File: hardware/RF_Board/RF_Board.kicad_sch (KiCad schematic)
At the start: 129 parts, among them J1 Conn_Coaxial, J2 Conn_01x04_Male, J3 Conn_Coaxial, J4 Conn_01x04_Male, J5 Conn_01x06_Female, J6 Conn_01x06_Female, J7 Conn_01x06_Female, J8 L77TSAH15SOL2RM8, J9 Conn_01x09_Male, Q1 2N7002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

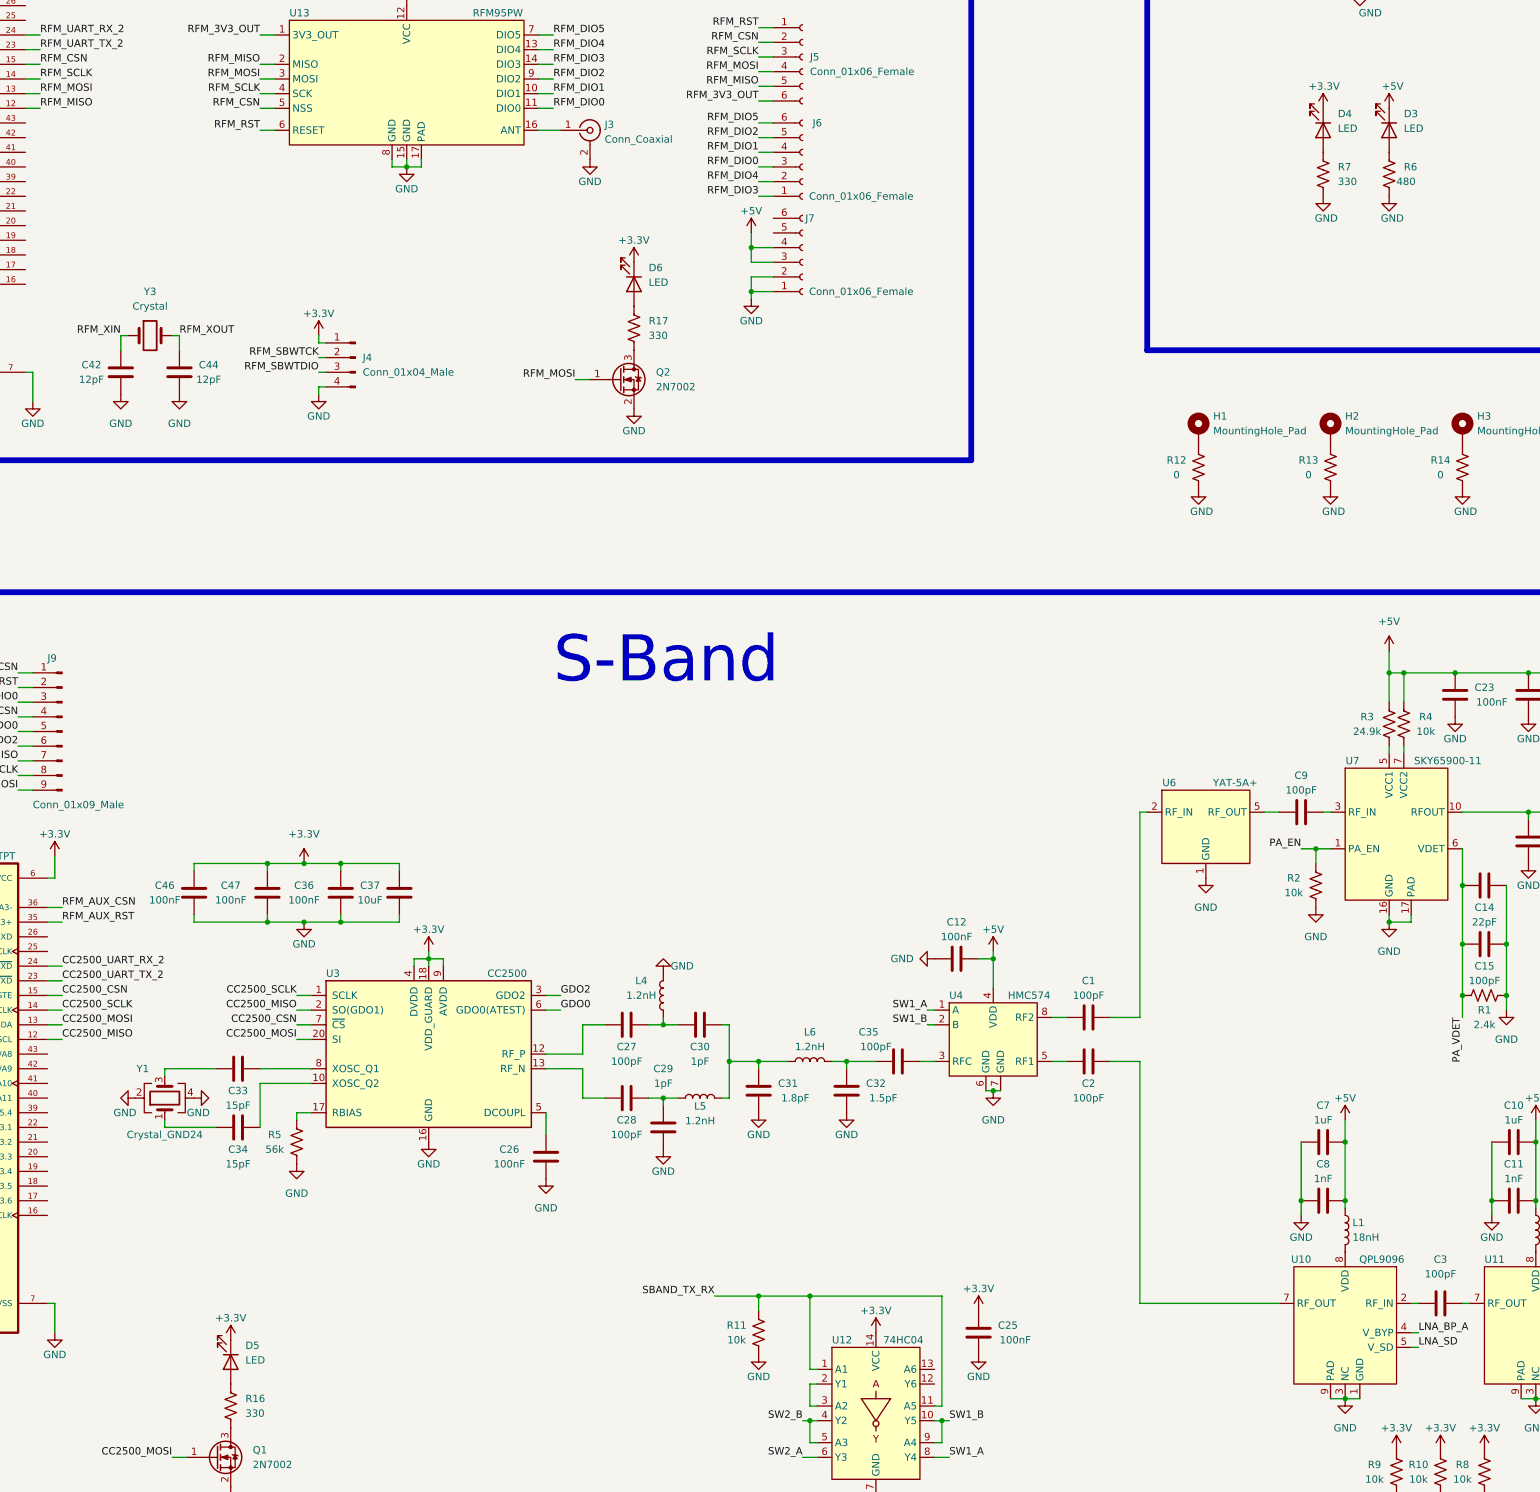
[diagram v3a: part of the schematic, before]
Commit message: fix LED polarity
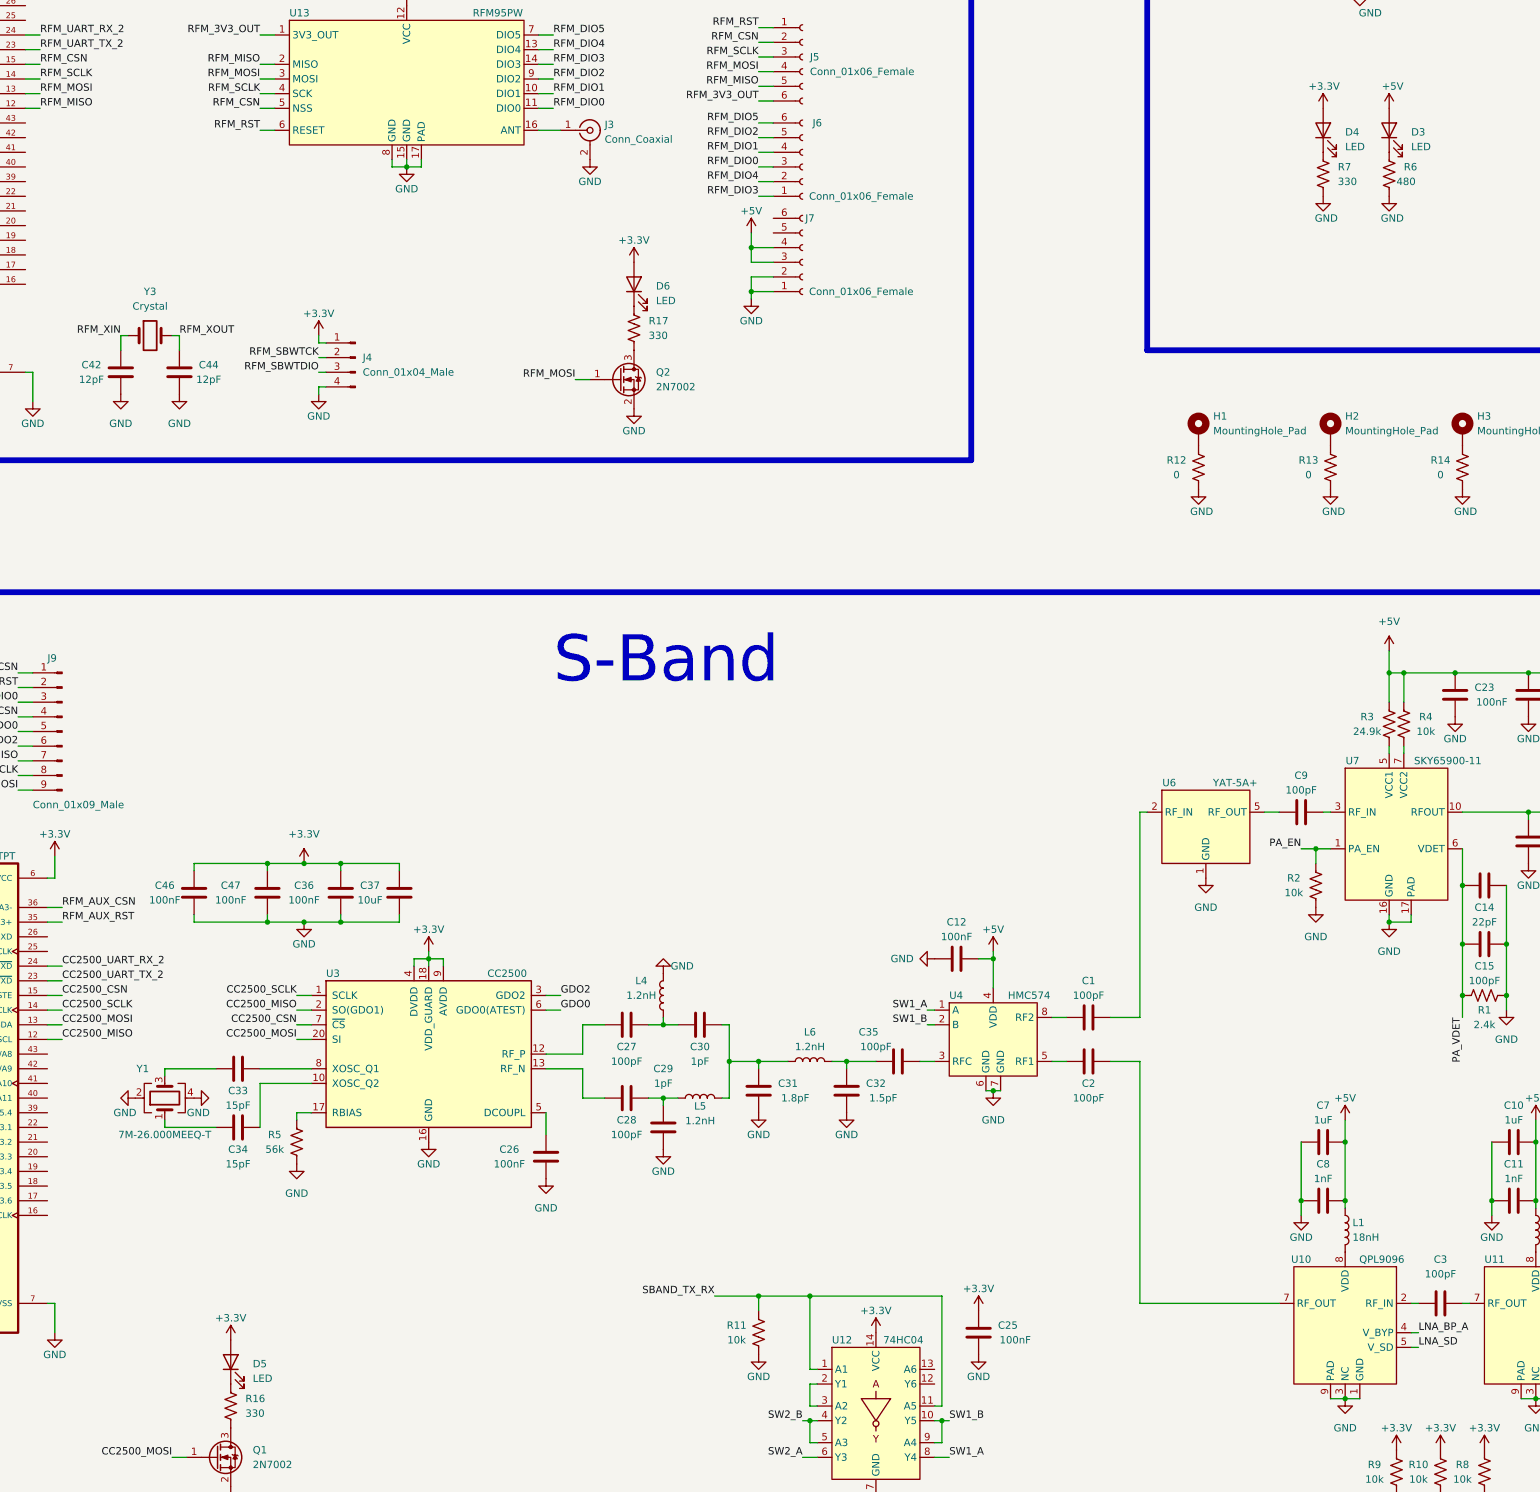
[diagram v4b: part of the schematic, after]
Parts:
- Y1: value Crystal_GND24 -> 7M-26.000MEEQ-T
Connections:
- net +3.3V: now also D4.2 (A), D5.2 (A), D6.2 (A); no longer D4.1 (K), D5.1 (K), D6.1 (K)
- net +5V: now also D3.2 (A); no longer D3.1 (K)
- net at R6.1: now also D3.1 (K); no longer D3.2 (A)
- net at R16.1: now also D5.1 (K); no longer D5.2 (A)
- net at R7.1: now also D4.1 (K); no longer D4.2 (A)
- net at R17.1: now also D6.1 (K); no longer D6.2 (A)
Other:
- moved on the sheet: D3, D4, D5, D6
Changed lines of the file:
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@@
     (pin "2")
   )
-  (symbol (lib_id "RF_Board_Symbols:LED") (at 422.91 101.6 270) (unit 1)
+  (symbol (lib_id "RF_Board_Symbols:LED") (at 422.91 101.6 90) (unit 1)
     (in_bom yes) (on_board yes) (fields_autoplaced)
-    (property "Reference" "D3" (id 0) (at 425.45 98.7424 90)
-      (effects (font (size 1.27 1.27)) (justify left))
+    (property "Reference" "D3" (id 0) (at 426.72 101.9174 90)
+      (effects (font (size 1.27 1.27)) (justify right))
     )
-    (property "Value" "LED" (id 1) (at 425.45 101.2824 90)
-      (effects (font (size 1.27 1.27)) (justify left))
+    (property "Value" "LED" (id 1) (at 426.72 104.4574 90)
+      (effects (font (size 1.27 1.27)) (justify right))
     )
     (property "Footprint" "RF_Board_Footprints:LED_0603_1608Metric" (id 2) (at 422.91 101.6 0)
@@
     (in_bom yes) (on_board yes)
     (property "Reference" "Y1" (id 0) (at 207.01 264.16 90))
-    (property "Value" "Crystal_GND24" (id 1) (at 210.82 275.59 90))
+    (property "Value" "7M-26.000MEEQ-T" (id 1) (at 210.82 275.59 90))
     (property "Footprint" "RF_Board_Footprints:Crystal_SMD_3225-4Pin_3.2x2.5mm" (id 2) (at 210.82 269.24 0)
       (effects (font (size 1.27 1.27)) hide)
@@
     (pin "2")
   )
-  (symbol (lib_id "RF_Board_Symbols:LED") (at 411.48 101.6 270) (unit 1)
+  (symbol (lib_id "RF_Board_Symbols:LED") (at 411.48 101.6 90) (unit 1)
     (in_bom yes) (on_board yes) (fields_autoplaced)
-    (property "Reference" "D4" (id 0) (at 414.02 98.7424 90)
-      (effects (font (size 1.27 1.27)) (justify left))
+    (property "Reference" "D4" (id 0) (at 415.29 101.9174 90)
+      (effects (font (size 1.27 1.27)) (justify right))
     )
-    (property "Value" "LED" (id 1) (at 414.02 101.2824 90)
-      (effects (font (size 1.27 1.27)) (justify left))
+    (property "Value" "LED" (id 1) (at 415.29 104.4574 90)
+      (effects (font (size 1.27 1.27)) (justify right))
     )
     (property "Footprint" "RF_Board_Footprints:LED_0603_1608Metric" (id 2) (at 411.48 101.6 0)
@@
     (pin "1")
   )
-  (symbol (lib_id "RF_Board_Symbols:LED") (at 292.1 128.27 270) (unit 1)
+  (symbol (lib_id "RF_Board_Symbols:LED") (at 292.1 128.27 90) (unit 1)
     (in_bom yes) (on_board yes) (fields_autoplaced)
-    (property "Reference" "D6" (id 0) (at 294.64 125.4124 90)
-      (effects (font (size 1.27 1.27)) (justify left))
+    (property "Reference" "D6" (id 0) (at 295.91 128.5874 90)
+      (effects (font (size 1.27 1.27)) (justify right))
     )
-    (property "Value" "LED" (id 1) (at 294.64 127.9524 90)
-      (effects (font (size 1.27 1.27)) (justify left))
+    (property "Value" "LED" (id 1) (at 295.91 131.1274 90)
+      (effects (font (size 1.27 1.27)) (justify right))
     )
     (property "Footprint" "RF_Board_Footprints:LED_0603_1608Metric" (id 2) (at 292.1 128.27 0)
@@
     (pin "2")
   )
-  (symbol (lib_id "RF_Board_Symbols:LED") (at 222.25 314.96 270) (unit 1)
+  (symbol (lib_id "RF_Board_Symbols:LED") (at 222.25 314.96 90) (unit 1)
     (in_bom yes) (on_board yes) (fields_autoplaced)
-    (property "Reference" "D5" (id 0) (at 224.79 312.1024 90)
-      (effects (font (size 1.27 1.27)) (justify left))
+    (property "Reference" "D5" (id 0) (at 226.06 315.2774 90)
+      (effects (font (size 1.27 1.27)) (justify right))
     )
-    (property "Value" "LED" (id 1) (at 224.79 314.6424 90)
-      (effects (font (size 1.27 1.27)) (justify left))
+    (property "Value" "LED" (id 1) (at 226.06 317.8174 90)
+      (effects (font (size 1.27 1.27)) (justify right))
     )
     (property "Footprint" "RF_Board_Footprints:LED_0603_1608Metric" (id 2) (at 222.25 314.96 0)
@@
     )
     (path "/2e2c2d33-fba7-4ab8-92e0-d611208419ce"
-      (reference "Y1") (unit 1) (value "Crystal_GND24") (footprint "RF_Board_Footprints:Crystal_SMD_3225-4Pin_3.2x2.5mm")
+      (reference "Y1") (unit 1) (value "7M-26.000MEEQ-T") (footprint "RF_Board_Footprints:Crystal_SMD_3225-4Pin_3.2x2.5mm")
     )
     (path "/b1e13d1d-1049-4af9-bbdf-669677daba83"

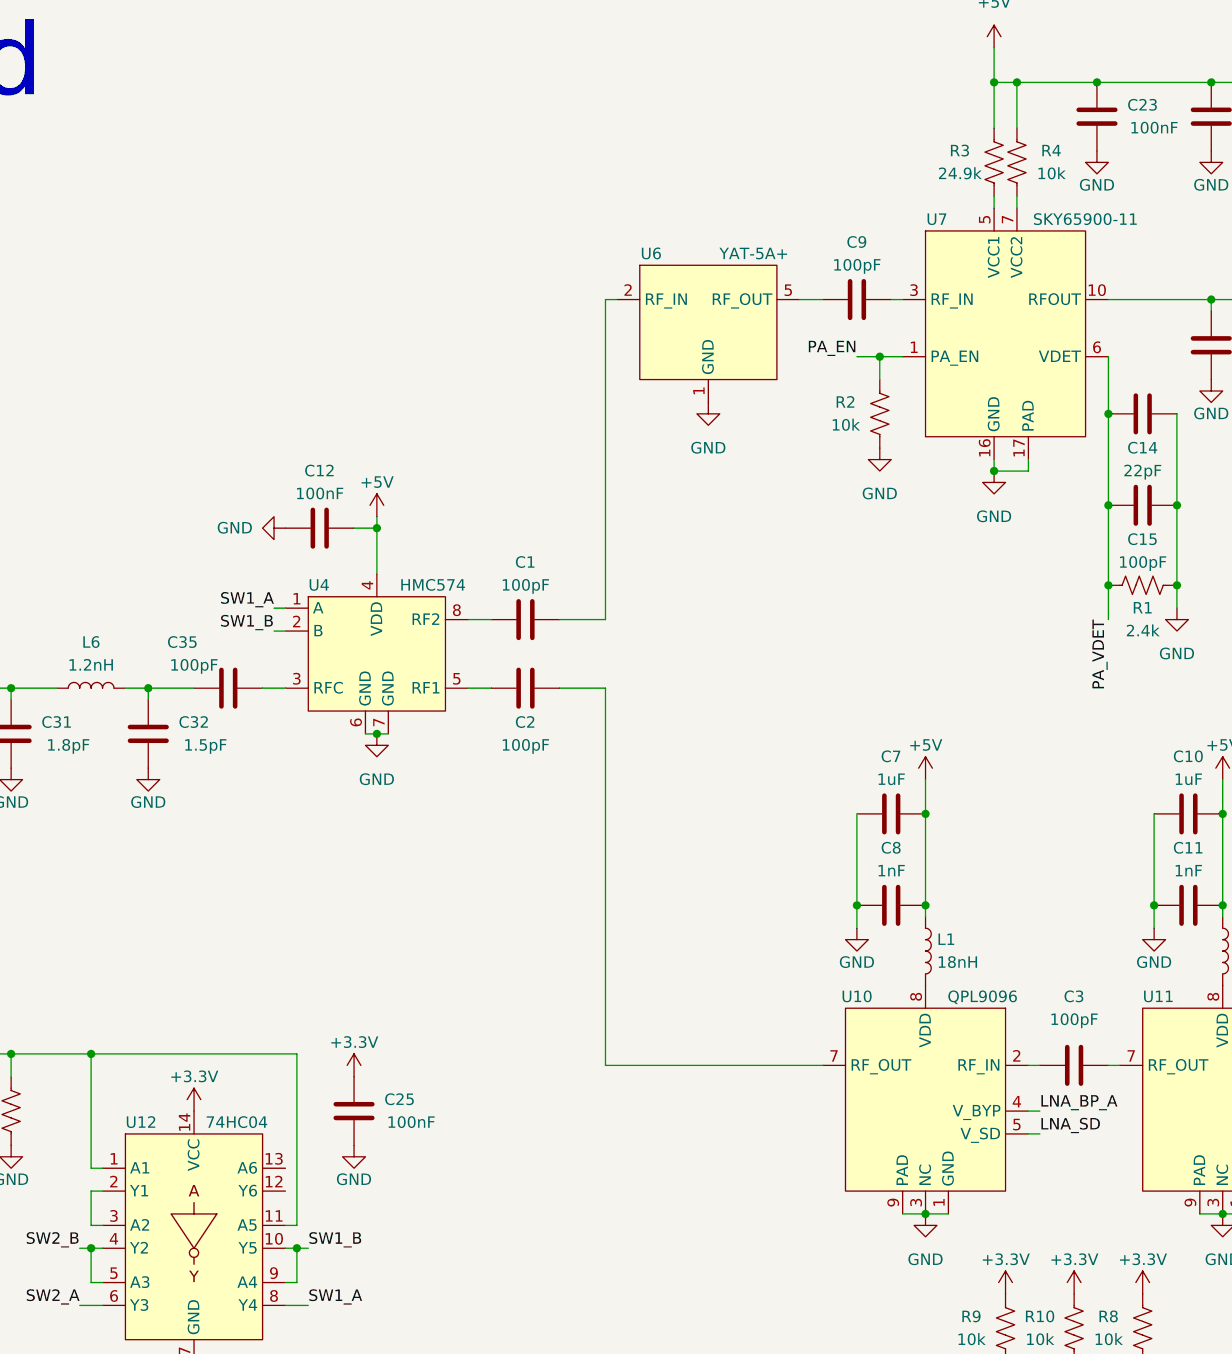
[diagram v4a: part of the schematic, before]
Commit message: respond to RF board feedback
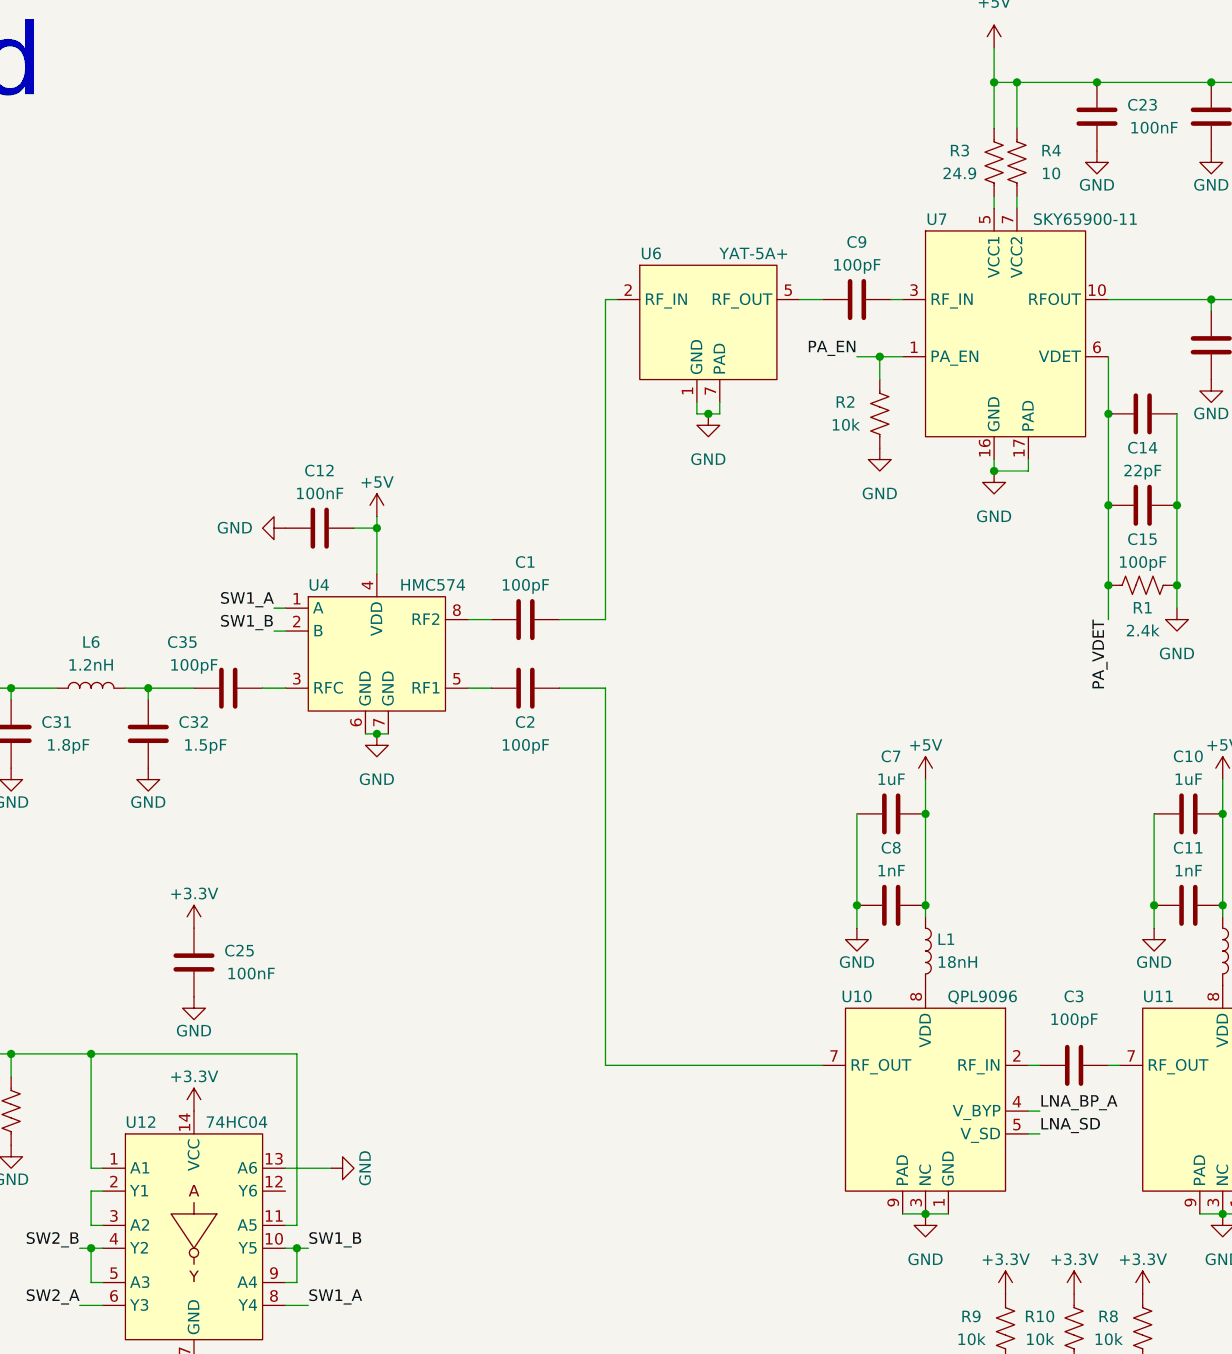
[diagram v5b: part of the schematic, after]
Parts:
- R3: value 24.9k -> 24.9
- R4: value 10k -> 10
- U1, U2: footprint RF_Board_Footprints:QFP50P900X900X160-48N -> QFP50P900X900X160-48N
- U14, U15: footprint RF_Board_Footprints:TPS259573DSGR -> DSG0008A
- U3: footprint RF_Board_Footprints:Texas_S-PVQFN-N20_EP2.4x2.4mm -> Package_DFN_QFN:Texas_S-PVQFN-N20_EP2.4x2.4mm
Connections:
- net GND: now also U12.13 (A6), U6.7 (PAD)
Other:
- moved on the sheet: C25
